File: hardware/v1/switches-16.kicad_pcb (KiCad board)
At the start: 2 copper layers, 200.7 x 34.3 mm, 18 parts, among them P1 CONN_02X02, SW1 SWITCH_INV, SW10 SWITCH_INV, SW11 SWITCH_INV, SW12 SWITCH_INV, SW13 SWITCH_INV, SW14 SWITCH_INV, SW15 SWITCH_INV, SW16 SWITCH_INV, SW2 SWITCH_INV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

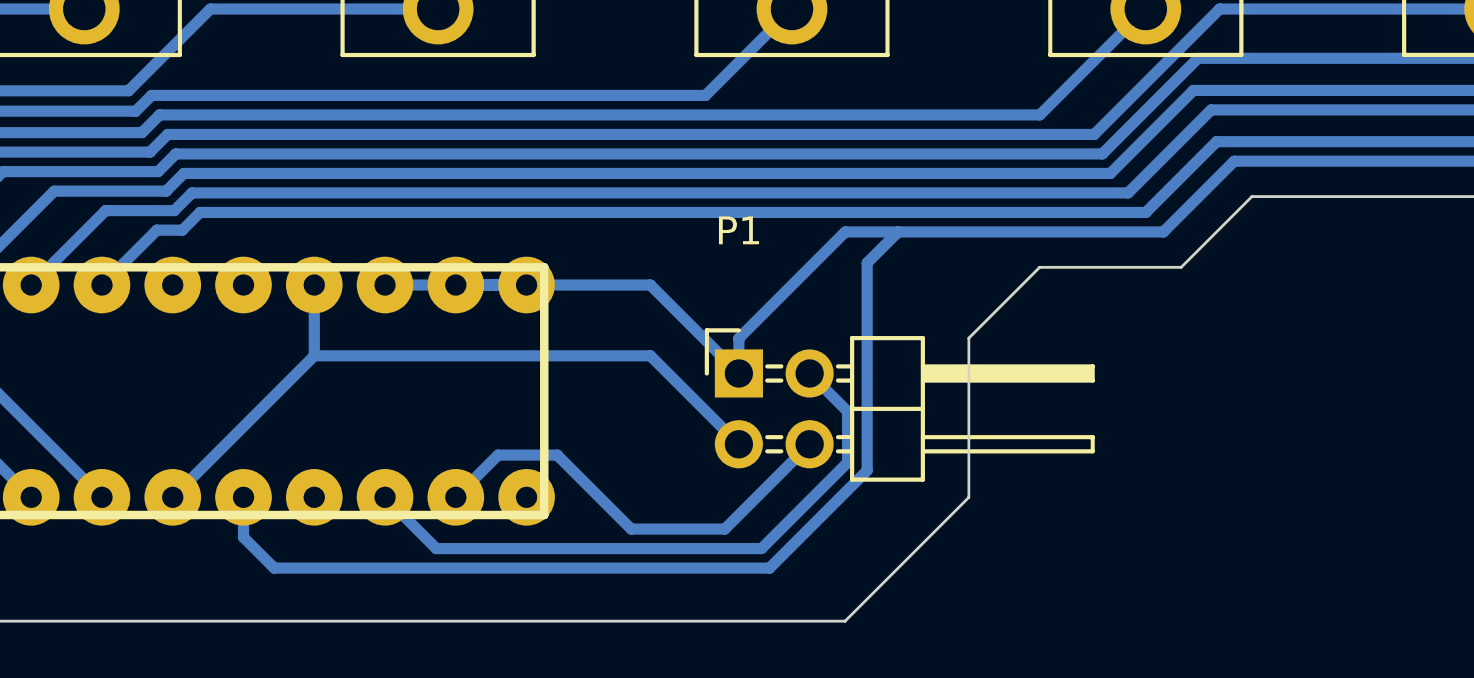
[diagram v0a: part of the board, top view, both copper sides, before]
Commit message: Re-arrange switch connector pinout to simpler single-row header. Re-route the switch boards accordingly.
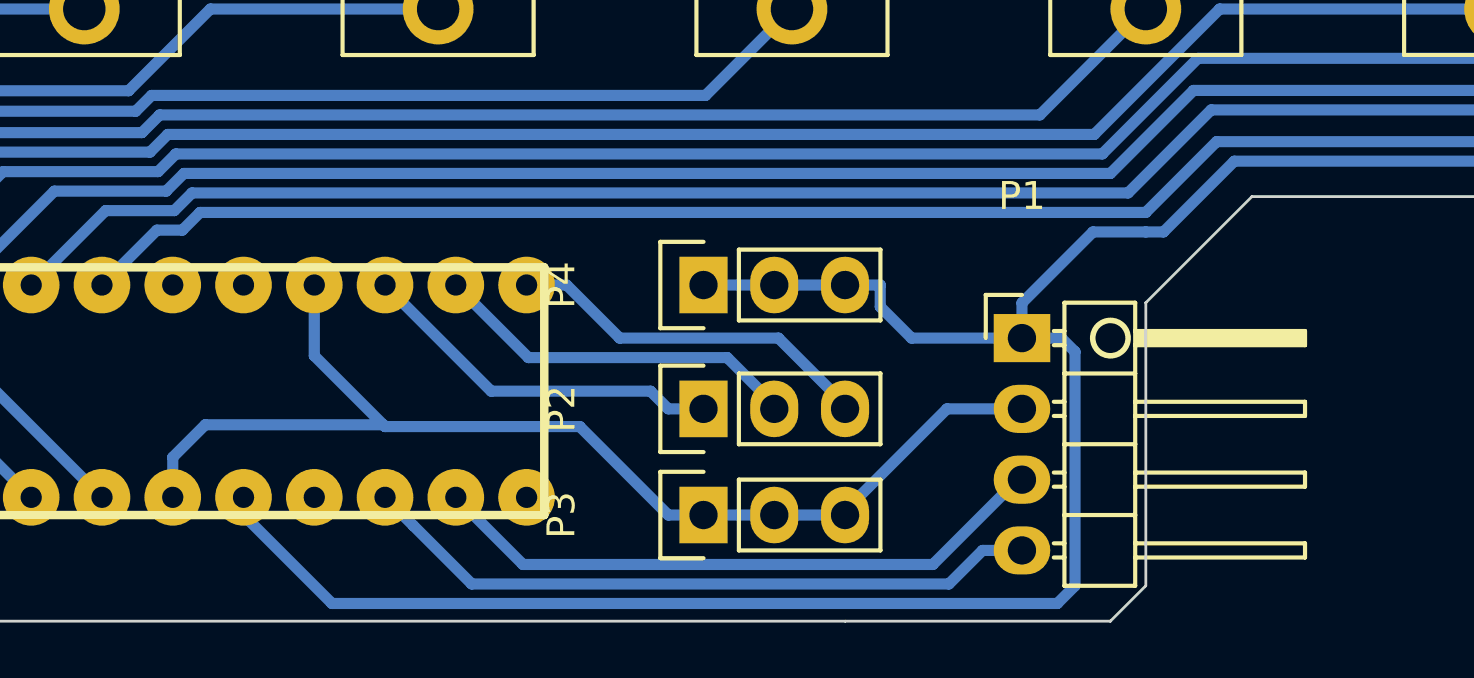
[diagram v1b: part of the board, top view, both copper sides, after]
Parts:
- added P2: CONN_01X03, Pin_Headers:Pin_Header_Straight_1x03, F.Cu at (187.3, 43.2)
- added P3: CONN_01X03, Pin_Headers:Pin_Header_Straight_1x03, F.Cu at (187.3, 47.0)
- added P4: CONN_01X03, Pin_Headers:Pin_Header_Straight_1x03, F.Cu at (187.3, 38.7)
- P1: value CONN_02X02 -> CONN_01X04; footprint Pin_Headers:Pin_Header_Angled_2x02 -> Pin_Headers:Pin_Header_Angled_1x04
- moved P1 10.2 mm to (198.8, 40.6)
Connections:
- P1 pad 2: /SCK -> VDD
- P1 pad 3: VDD -> /SDA
- P1 pad 4: /SDA -> /SCK
- SW1 pad 1: Net-(SW1-Pad1) -> (no net)
- SW10 pad 1: Net-(SW10-Pad1) -> (no net)
- SW11 pad 1: Net-(SW11-Pad1) -> (no net)
- SW12 pad 1: Net-(SW12-Pad1) -> (no net)
- SW13 pad 1: Net-(SW13-Pad1) -> (no net)
- SW14 pad 1: Net-(SW14-Pad1) -> (no net)
- SW15 pad 1: Net-(SW15-Pad1) -> (no net)
- SW16 pad 1: Net-(SW16-Pad1) -> (no net)
- SW2 pad 1: Net-(SW2-Pad1) -> (no net)
- SW3 pad 1: Net-(SW3-Pad1) -> (no net)
- SW4 pad 1: Net-(SW4-Pad1) -> (no net)
- SW5 pad 1: Net-(SW5-Pad1) -> (no net)
- SW6 pad 1: Net-(SW6-Pad1) -> (no net)
- SW7 pad 1: Net-(SW7-Pad1) -> (no net)
- SW8 pad 1: Net-(SW8-Pad1) -> (no net)
- SW9 pad 1: Net-(SW9-Pad1) -> (no net)
- U1 pad 11: Net-(U1-Pad11) -> (no net)
- U1 pad 14: Net-(U1-Pad14) -> (no net)
- U1 pad 15: GND -> Net-(P2-Pad3)
- U1 pad 16: GND -> Net-(P2-Pad2)
- U1 pad 17: GND -> Net-(P2-Pad1)
- U1 pad 19: Net-(U1-Pad19) -> (no net)
- U1 pad 20: Net-(U1-Pad20) -> (no net)
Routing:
- net VDD: track 26.3 -> 41.5 mm
- net Net-(P2-Pad3): track 0.00 -> 13.4 mm
- net Net-(P2-Pad2): track 0.00 -> 13.4 mm
- net Net-(P2-Pad1): track 0.00 -> 13.3 mm
- net /SDA: track 15.7 -> 22.6 mm
- net GND: track 540.0 -> 533.2 mm
- net /SCK: track 22.4 -> 24.6 mm
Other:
- outline, holes or cut-outs redrawn
